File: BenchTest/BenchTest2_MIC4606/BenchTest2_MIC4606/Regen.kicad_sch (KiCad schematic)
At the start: 15 parts, among them Q3 Q_PMOS_DGS, Q4 Q_PMOS_DGS, U4 TLP2767

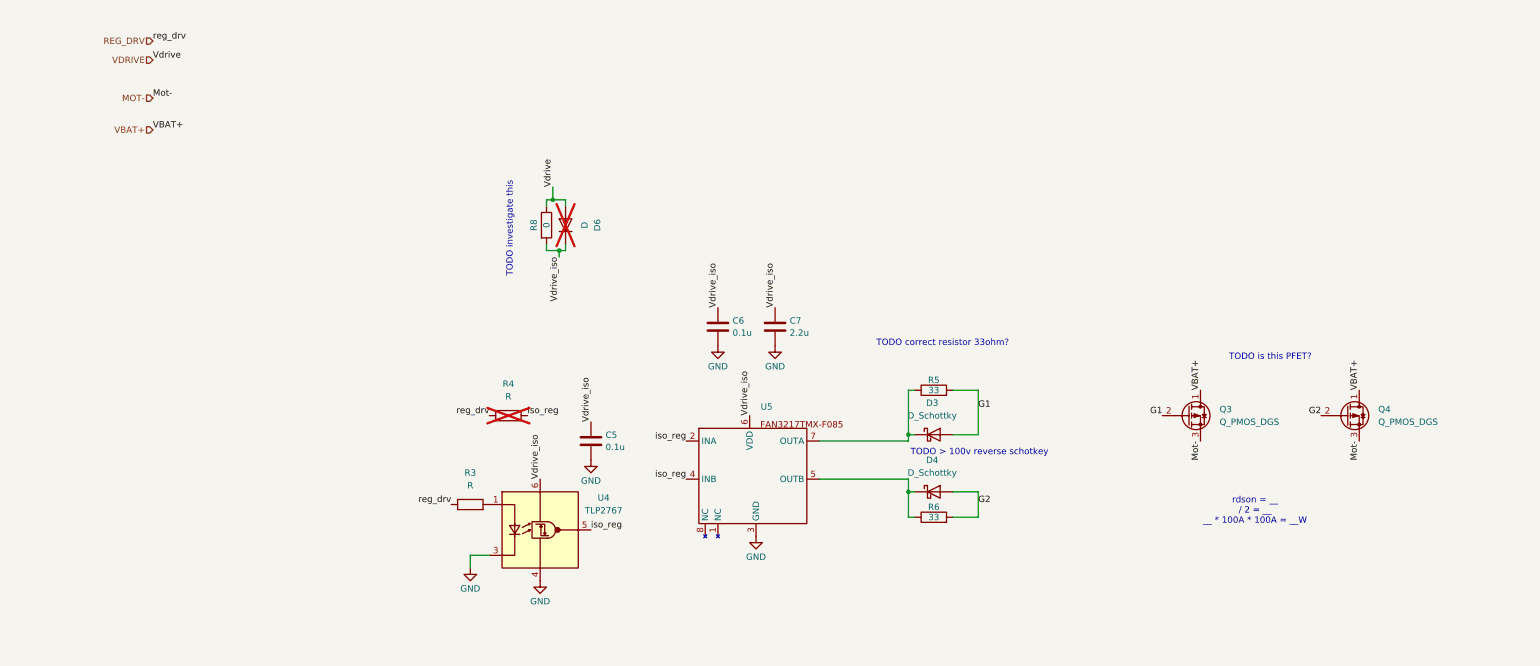
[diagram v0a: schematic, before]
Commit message: Defined Some parts, added notes for Arm/regen/H bridge
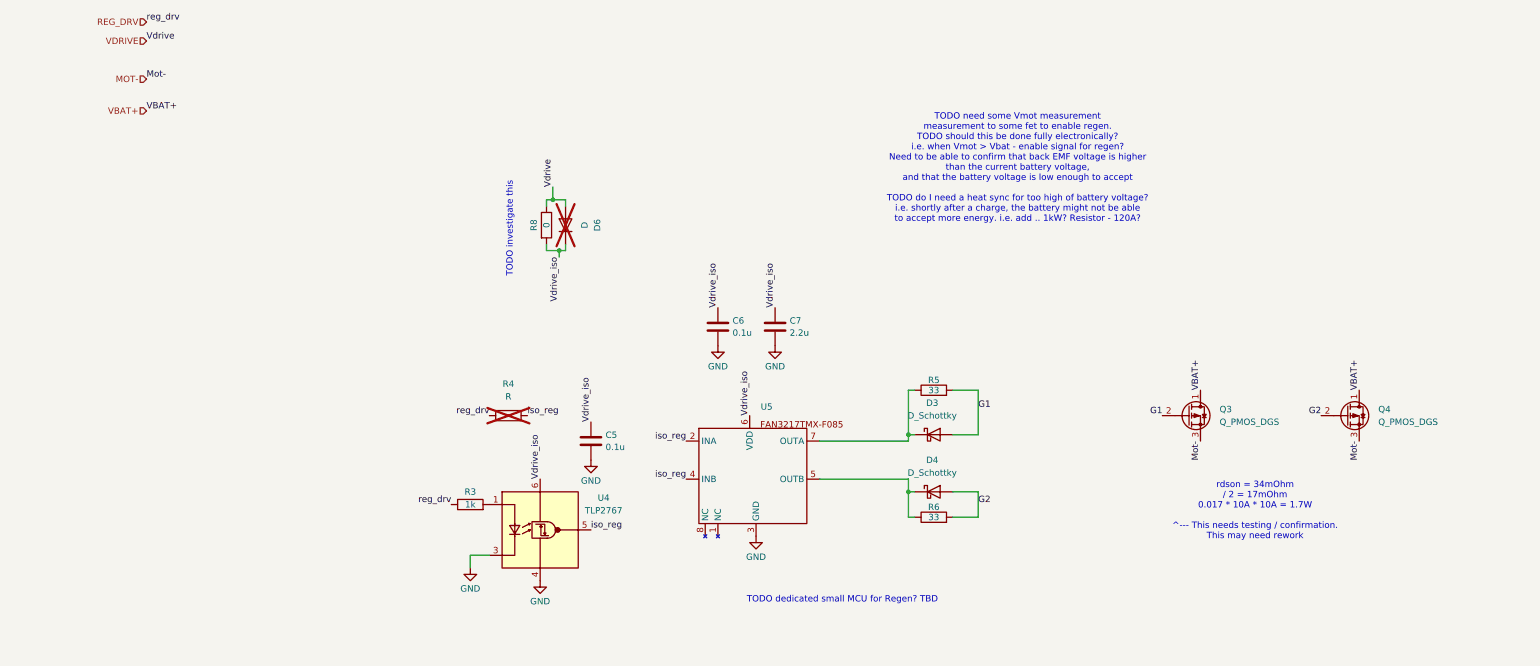
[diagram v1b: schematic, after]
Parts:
- R3: value R -> 1k
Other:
- note added: "TODO dedicated small MCU for Regen? TBD"
- note added: "TODO need some Vmot measurement measurement to some fet to enable regen. TODO should this be done fully electronically? i.e. when Vmot > Vbat - enable signal for regen? Need to be able to confirm that back EMF voltage is higher than the current battery voltage, and that the battery voltage is low enough to accept TODO do I need a heat sync for too high of battery voltage? i.e. shortly after a cha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"
- note added: "rdson = 34mOhm / 2 = 17mOhm 0.017 * 10A * 10A = 1.7W ^--- This needs testing / confirmation. This may need rework"
- note removed: "TODO > 100v reverse schotkey"
- note removed: "TODO correct resistor 33ohm?"
- note removed: "TODO is this PFET?"
- note removed: "rdson = __ / 2 = __ __ * 100A * 100A = __W"
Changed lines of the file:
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@@
 	(generator_version "9.0")
 	(paper "A4")
-	(text "TODO is this PFET?"
-		(exclude_from_sim no)
-		(at 248.92 83.566 0)
-		(effects
-			(font
-				(size 1.27 1.27)
-			)
-		)
-	)
-	(text "TODO > 100v reverse schotkey"
-		(exclude_from_sim no)
-		(at 190.754 102.616 0)
-		(effects
-			(font
-				(size 1.27 1.27)
-			)
-		)
-	)
-	(text "TODO correct resistor 33ohm?"
-		(exclude_from_sim no)
-		(at 183.388 80.772 0)
+	(text "TODO need some Vmot measurement\nmeasurement to some fet to enable regen.\nTODO should this be done fully electronically? \ni.e. when Vmot > Vbat - enable signal for regen?\nNeed to be able to confirm that back EMF voltage is higher\nthan the current battery voltage,\nand that the battery voltage is low enough to accept\n\nTODO do I need a heat sync for too high of battery voltage?\ni.e. shortly after a charge, the battery might not be able\nto accept more energy. i.e. add .. 1kW? Resistor - 120A?"
+		(exclude_from_sim no)
+		(at 198.374 45.72 0)
 		(effects
 			(font
@@
 		)
 	)
-	(text "rdson = __\n/ 2 = __\n__ * 100A * 100A = __W "
+	(text "rdson = 34mOhm\n/ 2 = 17mOhm\n0.017 * 10A * 10A = 1.7W\n\n^--- This needs testing / confirmation.\nThis may need rework"
 		(exclude_from_sim no)
 		(at 245.872 114.3 0)
+		(effects
+			(font
+				(size 1.27 1.27)
+			)
+		)
+	)
+	(text "TODO dedicated small MCU for Regen? TBD"
+		(exclude_from_sim no)
+		(at 163.322 132.08 0)
 		(effects
 			(font
@@
 	)
 	(label "Vdrive"
-		(at 25.4 24.13 0)
+		(at 24.13 20.32 0)
 		(effects
 			(font
@@
 	)
 	(label "VBAT+"
-		(at 25.4 38.1 0)
+		(at 24.13 34.29 0)
 		(effects
 			(font
@@
 	)
 	(label "Mot-"
-		(at 25.4 31.75 0)
+		(at 24.13 27.94 0)
 		(effects
 			(font
@@
 	)
 	(label "reg_drv"
-		(at 25.4 20.32 0)
+		(at 24.13 16.51 0)
 		(effects
 			(font
@@
 	(hierarchical_label "VBAT+"
 		(shape input)
-		(at 25.4 38.1 180)
+		(at 24.13 34.29 180)
 		(effects
 			(font
@@
 	(hierarchical_label "REG_DRV"
 		(shape input)
-		(at 25.4 20.32 180)
+		(at 24.13 16.51 180)
 		(effects
 			(font
@@
 	(hierarchical_label "VDRIVE"
 		(shape input)
-		(at 25.4 24.13 180)
+		(at 24.13 20.32 180)
 		(effects
 			(font
@@
 	(hierarchical_label "MOT-"
 		(shape input)
-		(at 25.4 31.75 180)
+		(at 24.13 27.94 180)
 		(effects
 			(font
@@
 			)
 		)
-		(property "Description" "P-MOSFET transistor, drain/gate/source"
+		(property "Description" "RS1P090ATTB1"
 			(at 264.16 95.25 0)
 			(effects
@@
 			)
 		)
-		(property "Description" "P-MOSFET transistor, drain/gate/source"
+		(property "Description" "RS1P090ATTB1"
 			(at 232.41 95.25 0)
 			(effects
@@
 		(on_board yes)
 		(dnp no)
-		(fields_autoplaced yes)
 		(property "Reference" "R3"
-			(at 88.9 106.68 90)
-			(effects
-				(font
-					(size 1.27 1.27)
-				)
-			)
-		)
-		(property "Value" "R"
-			(at 88.9 109.22 90)
-			(effects
-				(font
+			(at 88.9 110.49 90)
+			(effects
+				(font
+					(size 1.27 1.27)
+				)
+			)
+		)
+		(property "Value" "1k"
+			(at 88.9 113.03 90)
+			(effects
+				(font

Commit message: Additional Documents / Routing
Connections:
- net MOT- renamed Mot-
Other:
- note added: "TODO is this right?"
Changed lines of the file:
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@@
+		)
+	)
+	(text "TODO is this right?"
+		(exclude_from_sim no)
+		(at 248.158 76.454 0)
+		(effects
+			(font
+				(size 1.27 1.27)
+			)
 		)
 	)
@@
 	)
 	(label "VBAT+"
-		(at 24.13 34.29 0)
+		(at 24.13 25.4 0)
 		(effects
 			(font
@@
 		)
 	)
-	(label "Mot-"
-		(at 24.13 27.94 0)
-		(effects
-			(font
-				(size 1.27 1.27)
-			)
-			(justify left bottom)
-		)
-	)
 	(label "G1"
 		(at 227.33 95.25 180)
@@
 	(hierarchical_label "VBAT+"
 		(shape input)
-		(at 24.13 34.29 180)
+		(at 24.13 25.4 180)
 		(effects
 			(font
@@
 		(effects
 			(font
-				(size 1.27 1.27)
-			)
-			(justify right)
-		)
-	)
-	(hierarchical_label "MOT-"
-		(shape input)
-		(at 24.13 27.94 180)
-		(effects
-			(font

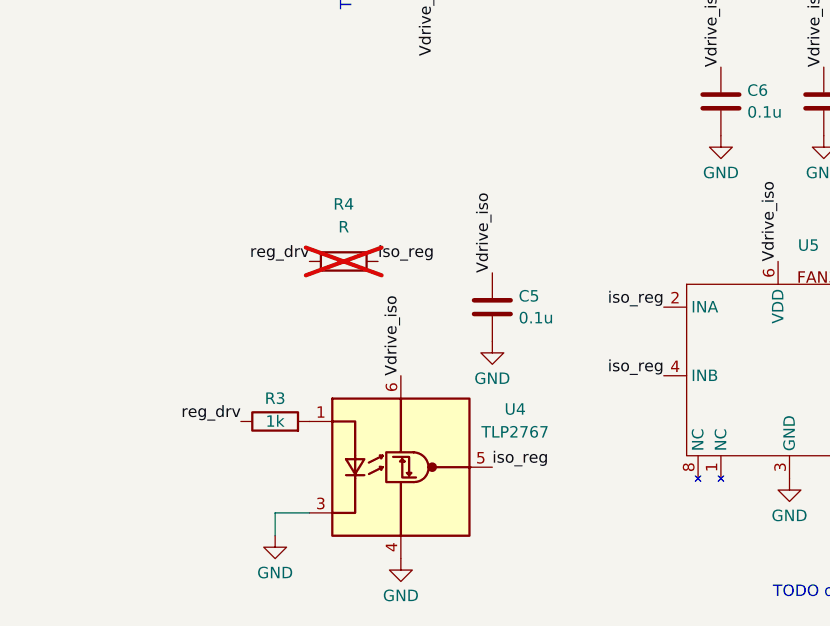
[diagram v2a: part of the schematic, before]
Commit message: Removed Optoisolators from digital Signals
Will be requiring these on the drive side
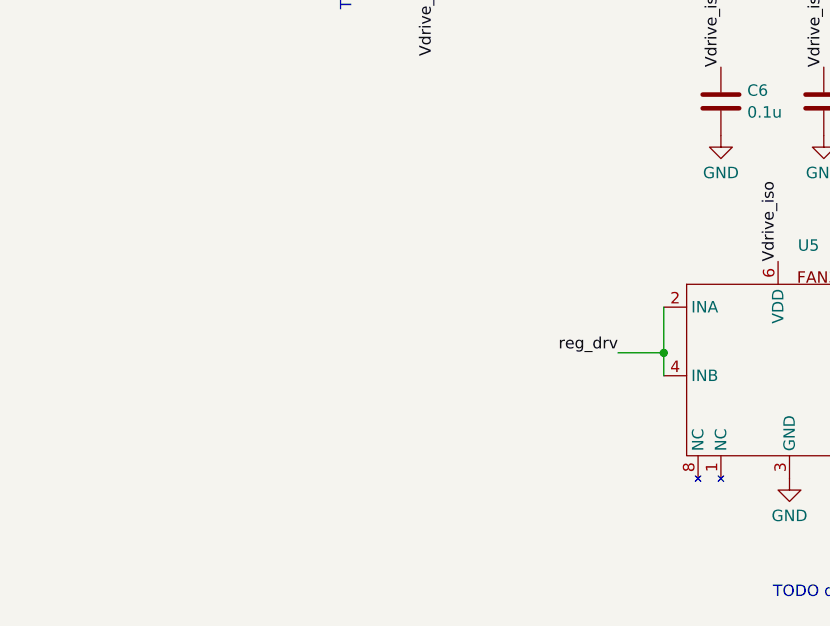
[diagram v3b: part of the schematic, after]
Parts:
- removed C5: 0.1u, Capacitor_SMD:C_0402_1005Metric_Pad0.74x0.62mm_HandSolder, symbol Device:C
- removed R3: 1k, symbol Device:R
- removed R4: R, symbol Device:R
- removed U4: TLP2767, Package_SO:SO-6L_10x3.84mm_P1.27mm, symbol Isolator:TLP2767
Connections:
- net iso_reg is gone; now on net REG_DRV: U5.2 (INA), U5.4 (INB)

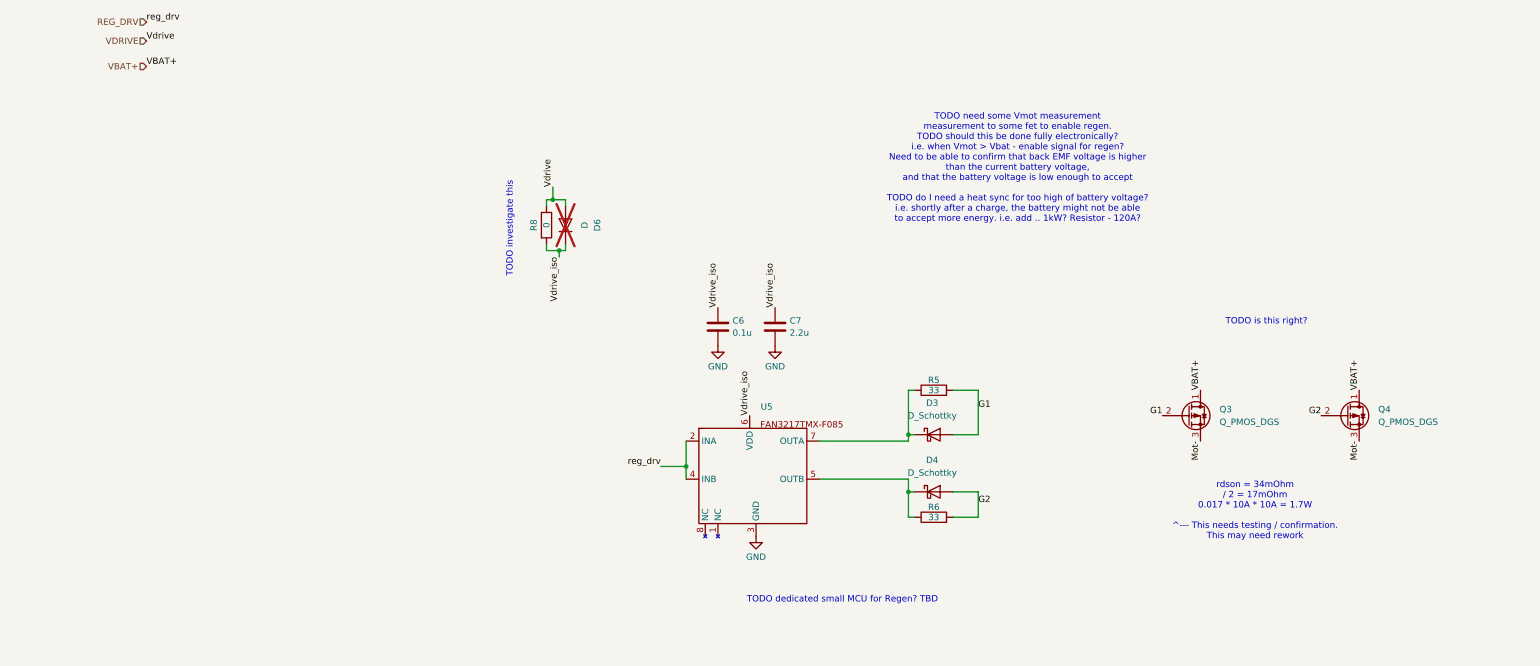
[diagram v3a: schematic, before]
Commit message: Assigned HP Footprints
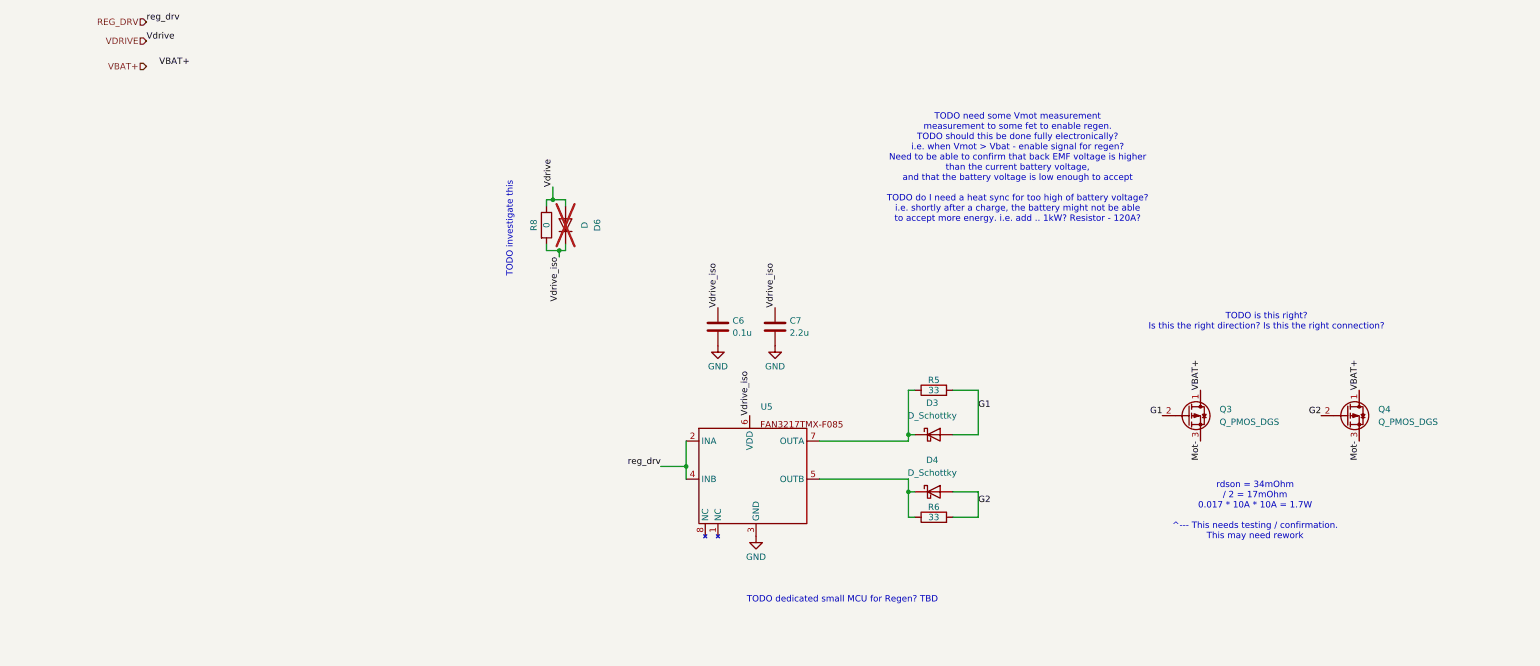
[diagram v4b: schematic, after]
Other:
- note added: "TODO is this right? Is this the right direction? Is this the right connection?"
- note removed: "TODO is this right?"
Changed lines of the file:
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@@
 		)
 	)
-	(text "TODO is this right?"
+	(text "TODO is this right?\nIs this the right direction? Is this the right connection?"
 		(exclude_from_sim no)
 		(at 248.158 76.454 0)
@@
 	)
 	(label "VBAT+"
-		(at 24.13 25.4 0)
+		(at 234.95 90.17 90)
 		(effects
 			(font
@@
 	)
 	(label "VBAT+"
-		(at 234.95 90.17 90)
-		(effects
-			(font
+		(at 26.67 25.4 0)
+		(effects
+			(font
